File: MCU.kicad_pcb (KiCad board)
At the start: 4 copper layers, 110.3 x 131.5 mm, 135 parts, among them J1 HSEC8-150-01-X-RA-X, J10 Conn_02x10_Odd_Even, J11 Conn_01x10, J12 Conn_01x10, J13 Conn_01x10, J14 Conn_01x10, J15 Conn_01x02, J16 Conn_02x10_Odd_Even, J17 Conn_02x30_Counter_Clockwise, J18 Conn_01x10, J19 Conn_01x10, J2 Barrel_Jack_MountingPin, J20 Conn_01x02, J21 Conn_02x10_Odd_Even, J22 Conn_01x02, J32 Conn_01x02, J4 Conn_02x30_Counter_Clockwise, J5 Conn_02x10_Odd_Even, J6 Conn_01x02, J7 Conn_01x10, J8 Conn_01x10, J9 Conn_01x02, U1 TPS76333, U10 TXB0104RUT, U11 TPS76333, U12 TXB0104RUT, U13 TXB0104RUT, U14 TPS76333, U2 TXB0104RUT, U3 LMR36510ADDA, U5 TXB0104RUT, U6 TXB0104RUT, U7 TXB0104RUT, U8 TPS76333, U9 TXB0104RUT

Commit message: Ready for review
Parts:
- removed R13, R14, R15, R16, R17, R18, R19, R20, R21, R22, R23, R24, R25, R26, R27, R28, R44, R47, R50, R52, R53, R54, R55, R56, R69, R70, R71, R72, R73, R74, R75, R76: 0R, Resistor_SMD:R_0201_0603Metric
- added H6: MountingHole_Pad, MountingHole:MountingHole_2.2mm_M2_DIN965_Pad, F.Cu at (184.5, 149.0)
- added J23: Conn_01x02, Connector_PinHeader_2.54mm:PinHeader_1x02_P2.54mm_Vertical, F.Cu at (156.3, 136.3)
- moved H1 63.8 mm to (94.5, 147.5)
- moved H4 2.55 mm to (157.0, 146.5)
- moved H5 2.50 mm to (84.5, 147.5)
- moved J2 1.00 mm to (137.5, 140.5)
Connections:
- J1 pad 16: unconnected-(J1-Pad16) -> A0V
- J1 pad 20: BTN_TRIP_TEST -> unconnected-(J1-Pad20)
- J1 pad 28: unconnected-(J1-Pad28) -> A0V
- J1 pad 29: unconnected-(J1-Pad29) -> A0V
- J1 pad 35: unconnected-(J1-Pad35) -> A0V
- J1 pad 59: unconnected-(J1-Pad59) -> A0V
- J1 pad 62: unconnected-(J1-Pad62) -> A0V
- J1 pad 68: unconnected-(J1-Pad68) -> A0V
- J1 pad 74: unconnected-(J1-Pad74) -> A0V
- J1 pad 78: unconnected-(J1-Pad78) -> A0V
- J1 pad 88: unconnected-(J1-Pad88) -> A0V
- J1 pad 91: unconnected-(J1-Pad91) -> A0V
- J1 pad 94: unconnected-(J1-Pad94) -> A0V
- J17 pad 26: /GP_SUB3/TP7_Pin11 -> /GP_SUB3/P11
- J17 pad 27: /GP_SUB3/TP15_Pin12 -> /GP_SUB3/P12
- J17 pad 28: /GP_SUB3/TP8_Pin13 -> /GP_SUB3/P13
- J17 pad 5: /GP_SUB2/TP7_Pin11 -> /GP_SUB2/P11
- J17 pad 6: /GP_SUB2/TP15_Pin12 -> /GP_SUB2/P12
- J17 pad 7: /GP_SUB2/TP8_Pin13 -> /GP_SUB2/P13
- J4 pad 38: BTN_TRIP_TEST -> unconnected-(J4-Pin_38-Pad38)
- J4 pad 5: /GP_SUB/TP7_Pin11 -> /GP_SUB/P11
- J4 pad 54: /GP_SUB1/TP8_Pin13 -> /GP_SUB1/P13
- J4 pad 55: /GP_SUB1/TP15_Pin12 -> /GP_SUB1/P12
- J4 pad 56: /GP_SUB1/TP7_Pin11 -> /GP_SUB1/P11
- J4 pad 6: /GP_SUB/TP15_Pin12 -> /GP_SUB/P12
- J4 pad 7: /GP_SUB/TP8_Pin13 -> /GP_SUB/P13
- U10 pad 10: /GP_SUB2/TP7_Pin11 -> unconnected-(U10-B1-Pad10)
- U10 pad 2: Net-(U10-A1) -> unconnected-(U10-A1-Pad2)
- U10 pad 3: Net-(U10-A2) -> /GP_SUB2/P9
- U10 pad 4: Net-(U10-A3) -> unconnected-(U10-A3-Pad4)
- U10 pad 5: Net-(U10-A4) -> /GP_SUB2/P8
- U10 pad 8: /GP_SUB2/TP8_Pin13 -> unconnected-(U10-B3-Pad8)
- U12 pad 2: Net-(U12-A1) -> /GP_SUB3/P14
- U12 pad 3: Net-(U12-A2) -> /GP_SUB3/P16
- U12 pad 4: Net-(U12-A3) -> unconnected-(U12-A3-Pad4)
- U12 pad 5: Net-(U12-A4) -> /GP_SUB3/P7
- U12 pad 8: /GP_SUB3/TP15_Pin12 -> unconnected-(U12-B3-Pad8)
- U13 pad 10: /GP_SUB3/TP7_Pin11 -> unconnected-(U13-B1-Pad10)
- U13 pad 2: Net-(U13-A1) -> unconnected-(U13-A1-Pad2)
- U13 pad 3: Net-(U13-A2) -> /GP_SUB3/P9
- U13 pad 4: Net-(U13-A3) -> unconnected-(U13-A3-Pad4)
- U13 pad 5: Net-(U13-A4) -> /GP_SUB3/P8
- U13 pad 8: /GP_SUB3/TP8_Pin13 -> unconnected-(U13-B3-Pad8)
- U2 pad 2: Net-(U2-A1) -> /GP_SUB/P14
- U2 pad 3: Net-(U2-A2) -> /GP_SUB/P16
- U2 pad 4: Net-(U2-A3) -> unconnected-(U2-A3-Pad4)
- U2 pad 5: Net-(U2-A4) -> /GP_SUB/P7
- U2 pad 8: /GP_SUB/TP15_Pin12 -> unconnected-(U2-B3-Pad8)
- U5 pad 10: /GP_SUB/TP7_Pin11 -> unconnected-(U5-B1-Pad10)
- U5 pad 2: Net-(U5-A1) -> unconnected-(U5-A1-Pad2)
- U5 pad 3: Net-(U5-A2) -> /GP_SUB/P9
- U5 pad 4: Net-(U5-A3) -> unconnected-(U5-A3-Pad4)
- U5 pad 5: Net-(U5-A4) -> /GP_SUB/P8
- U5 pad 8: /GP_SUB/TP8_Pin13 -> unconnected-(U5-B3-Pad8)
- U6 pad 2: Net-(U6-A1) -> /GP_SUB1/P14
- U6 pad 3: Net-(U6-A2) -> /GP_SUB1/P16
- U6 pad 4: Net-(U6-A3) -> unconnected-(U6-A3-Pad4)
- U6 pad 5: Net-(U6-A4) -> /GP_SUB1/P7
- U6 pad 8: /GP_SUB1/TP15_Pin12 -> unconnected-(U6-B3-Pad8)
- U7 pad 10: /GP_SUB1/TP7_Pin11 -> unconnected-(U7-B1-Pad10)
- U7 pad 2: Net-(U7-A1) -> unconnected-(U7-A1-Pad2)
- U7 pad 3: Net-(U7-A2) -> /GP_SUB1/P9
- U7 pad 4: Net-(U7-A3) -> unconnected-(U7-A3-Pad4)
- U7 pad 5: Net-(U7-A4) -> /GP_SUB1/P8
- U7 pad 8: /GP_SUB1/TP8_Pin13 -> unconnected-(U7-B3-Pad8)
- U9 pad 2: Net-(U9-A1) -> /GP_SUB2/P14
- U9 pad 3: Net-(U9-A2) -> /GP_SUB2/P16
- U9 pad 4: Net-(U9-A3) -> unconnected-(U9-A3-Pad4)
- U9 pad 5: Net-(U9-A4) -> /GP_SUB2/P7
- U9 pad 8: /GP_SUB2/TP15_Pin12 -> unconnected-(U9-B3-Pad8)
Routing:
- net BTN_TRIP_TEST: track 187.6 -> 0.00 mm, vias 3 -> 0
- net PADLOCK_OF: track 183.3 -> 237.6 mm, vias 1 -> 2
- net /GP_SUB/P13: track 29.4 -> 67.4 mm, vias 0 -> 1
- net /GP_SUB1/TP15_Pin12: track 36.5 -> 0.00 mm
- net /GP_SUB/P12: track 22.1 -> 53.6 mm, vias 0 -> 2
- net /GP_SUB1/P13: track 33.3 -> 64.6 mm, vias 0 -> 1
- net /GP_SUB/TP8_Pin13: track 31.0 -> 0.00 mm, vias 1 -> 0
- net /GP_SUB/P11: track 25.1 -> 56.0 mm, vias 0 -> 2
- net /GP_SUB3/P11: track 37.3 -> 66.8 mm, vias 0 -> 1
- net /GP_SUB1/TP8_Pin13: track 29.2 -> 0.00 mm, vias 1 -> 0
- net /GP_SUB/TP7_Pin11: track 29.2 -> 0.00 mm, vias 1 -> 0
- net /GP_SUB3/P12: track 57.1 -> 85.8 mm, vias 0 -> 2
- net /GP_SUB1/P11: track 28.9 -> 57.2 mm, vias 0 -> 1
- net /GP_SUB/TP15_Pin12: track 28.0 -> 0.00 mm, vias 1 -> 0
- net /GP_SUB3/TP7_Pin11: track 23.8 -> 0.00 mm, vias 1 -> 0
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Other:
- board size 110.3 x 131.5 mm -> 110.3 x 131 mm
- board text added: "P24V"
- board text added: "PADL"
- board text added: "SHLD GND"
- board text removed: "VBUS"

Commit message: For review
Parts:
- added TP1: TestPoint, TestPoint:TestPoint_Pad_1.5x1.5mm, F.Cu at (133.2, 133.9)
- R68, R8, R88, R92: value 1k -> 4k7
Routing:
- net Net-(U3-PG): track 3.57 -> 12.7 mm
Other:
- board text added: "5VPG"
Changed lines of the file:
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@@
 			)
 		)
-		(property "Value" "1k"
+		(property "Value" "4k7"
 			(at 0 1.43 90)
 			(layer "F.Fab")
@@
 		(tags "capacitor")
 		(property "Reference" "C35"
-			(at 4 0 180)
+			(at 4 -1 180)
 			(layer "F.SilkS")
 			(effects
@@
 			)
 		)
-		(property "Value" "1k"
+		(property "Value" "4k7"
 			(at 0 1.43 90)
 			(layer "F.Fab")
@@
 			)
 		)
-		(property "Value" "1k"
+		(property "Value" "4k7"
 			(at 0 1.43 90)
 			(layer "F.Fab")
@@
 		)
 	)
+	(footprint "TestPoint:TestPoint_Pad_1.5x1.5mm"
+		(layer "F.Cu")
+		(at 133.225 133.925)
+		(descr "SMD rectangular pad as test Point, square 1.5mm side length")
+		(tags "test point SMD pad rectangle square")
+		(property "Reference" "TP1"
+			(at 0 -1.648 0)
+			(layer "F.SilkS")
+			(effects
+				(font
+					(size 1 1)
+					(thickness 0.15)
+				)
+			)
+		)
+		(property "Value" "TestPoint"
+			(at 0 1.75 0)
+			(layer "F.Fab")
+			(effects
+				(font
+					(size 1 1)
+					(thickness 0.15)
+				)
+			)
+		)
+		(property "Datasheet" ""
+			(at 0 0 0)
+			(unlocked yes)
+			(layer "F.Fab")
+			(hide yes)
+			(effects
+				(font
+					(size 1.27 1.27)
+					(thickness 0.15)
+				)
+			)
+		)
+		(property "Description" "test point"
+			(at 0 0 0)
+			(unlocked yes)
+			(layer "F.Fab")
+			(hide yes)
+			(effects
+				(font
+					(size 1.27 1.27)
+					(thickness 0.15)
+				)
+			)
+		)
+		(property ki_fp_filters "Pin* Test*")
+		(sheetname "/")
+		(sheetfile "MCU.kicad_sch")
+		(units
+			(unit
+				(name "A")
+				(pins "1")
+			)
+		)
+		(duplicate_pad_numbers_are_jumpers no)
+		(fp_line
+			(start -0.95 -0.95)
+			(end 0.95 -0.95)
+			(stroke
+				(width 0.12)
+				(type solid)
+			)
+			(layer "F.SilkS")
+		)
+		(fp_line
+			(start -0.95 0.95)
+			(end -0.95 -0.95)
+			(stroke
+				(width 0.12)
+				(type solid)
+			)
+			(layer "F.SilkS")
+		)
+		(fp_line
+			(start 0.95 -0.95)
+			(end 0.95 0.95)
+			(stroke
+				(width 0.12)
+				(type solid)
+			)
+			(layer "F.SilkS")
+		)
+		(fp_line
+			(start 0.95 0.95)
+			(end -0.95 0.95)
+			(stroke
+				(width 0.12)
+				(type solid)
+			)
+			(layer "F.SilkS")
+		)
+		(fp_line
+			(start -1.25 -1.25)
+			(end -1.25 1.25)
+			(stroke
+				(width 0.05)
+				(type solid)
+			)
+			(layer "F.CrtYd")
+		)
+		(fp_line
+			(start -1.25 -1.25)
+			(end 1.25 -1.25)
+			(stroke
+				(width 0.05)
+				(type solid)
+			)
+			(layer "F.CrtYd")
+		)
+		(fp_line
+			(start 1.25 1.25)
+			(end -1.25 1.25)
+			(stroke
+				(width 0.05)
+				(type solid)
+			)
+			(layer "F.CrtYd")
+		)
+		(fp_line
+			(start 1.25 1.25)
+			(end 1.25 -1.25)
+			(stroke
+				(width 0.05)
+				(type solid)
+			)
+			(layer "F.CrtYd")
+		)
+		(fp_text user "${REFERENCE}"
+			(at 0 -1.65 0)
+			(layer "F.Fab")
+			(effects
+				(font
+					(size 1 1)
+					(thickness 0.15)
+				)
+			)
+		)
+		(pad "1" smd rect
+			(at 0 0)
+			(size 1.5 1.5)
+			(layers "F.Cu" "F.Mask")
+			(net "Net-(U3-PG)")
+			(pinfunction "1_1")
+			(pintype "passive")
+		)
+		(embedded_fonts no)
+	)
 	(footprint "Resistor_SMD:R_0603_1608Metric"
 		(layer "F.Cu")
@@
 		(tags "resistor")
 		(property "Reference" "R98"
-			(at -2.5 1.5 180)
+			(at -3.5 2 270)
 			(layer "F.SilkS")
 			(effects
@@
 			)
 		)
-		(property "Value" "1k"
+		(property "Value" "4k7"
 			(at 0 1.43 0)
 			(layer "F.Fab")
@@
 		)
 	)
+	(gr_text "5VPG"
+		(at 134.5 135 0)
+		(layer "F.SilkS")
+		(effects
+			(font
+				(size 1.5 1.5)
+				(thickness 0.3)
+				(bold yes)
+			)
+			(justify left bottom)
+		)
+	)
 	(gr_text "P24V"
 		(at 147.5 141 0)
@@
 	)
 	(segment
-		(start 127 137)
-		(end 127.5 136.5)
-		(width 0.5)
-		(layer "F.Cu")
-		(net "A0V")
-	)
-	(segment
 		(start 109.6 84.2)
 		(end 109.6 84.9375)
@@
 	)
 	(segment
-		(start 127 137.52)
-		(end 127 137)
-		(width 0.5)
-		(layer "F.Cu")
-		(net "A0V")
-	)
-	(segment
 		(start 98.5 36.2)
 		(end 98.5 35.640488)
@@
 	)
 	(segment
+		(start 127.5 136.5)
+		(end 127 137)
+		(width 0.5)
+		(layer "F.Cu")
+		(net "A0V")
+	)
+	(segment
 		(start 93.769 87.558476)
 		(end 94.431524 88.221)
@@
 	)
 	(segment
-		(start 125.5 135.675)
-		(end 126.675 135.675)
-		(width 0.5)
-		(layer "F.Cu")
-		(net "A0V")
-	)
-	(segment
 		(start 156.7105 81.2205)
 		(end 157.099 81.609)
@@
 	)
 	(segment
-		(start 126.675 135.675)
-		(end 127 136)
-		(width 0.5)
-		(layer "F.Cu")
-		(net "A0V")
-	)
-	(segment
 		(start 156.08326 113.912314)
 		(end 156.894074 113.1015)
@@
 	)
 	(segment
+		(start 127 135.35)
+		(end 126.675 135.675)
+		(width 0.5)
+		(layer "F.Cu")
+		(net "A0V")
+	)
+	(segment
 		(start 161.27676 103.689)
 		(end 161.27676 103.224)
@@
 	)
 	(segment
+		(start 126.675 135.675)
+		(end 125.5 135.675)
+		(width 0.5)
+		(layer "F.Cu")
+		(net "A0V")
+	)
+	(segment
 		(start 109.64 118.81)
 		(end 109.64 119.275)
@@
 	)
 	(segment
+		(start 127 135.08)
+		(end 127 135.35)
+		(width 0.5)
+		(layer "F.Cu")
+		(net "A0V")
+	)
+	(segment
 		(start 161.4625 83.2559)
 		(end 161.4625 84.3955)
@@
 	)
 	(segment
+		(start 127 137)
+		(end 127 137.52)
+		(width 0.5)
+		(layer "F.Cu")
+		(net "A0V")
+	)
+	(segment
 		(start 160.15 75.5)
 		(end 160.075 75.575)
@@
 	)
 	(via
-		(at 127 136)
+		(at 127 135.08)
 		(size 0.6)
 		(drill 0.3)
@@
 	)
 	(segment
+		(start 129.174533 133.925)
+		(end 125.774533 137.325)
+		(width 0.2)
+		(layer "F.Cu")
+		(net "Net-(U3-PG)")
+	)
+	(segment
 		(start 124.175 137.325)
 		(end 124 137.15)
@@
 		(layer "F.Cu")
 		(net "Net-(U3-PG)")
+	)
+	(segment
+		(start 133.225 133.925)
+		(end 129.174533 133.925)
+		(width 0.2)
+		(layer "F.Cu")
+		(net "Net-(U3-PG)")
+	)
+	(segment
+		(start 125.774533 137.325)
+		(end 125.5 137.325)
+		(width 0.2)
+		(layer "F.Cu")
+		(net "Net-(U3-PG)")

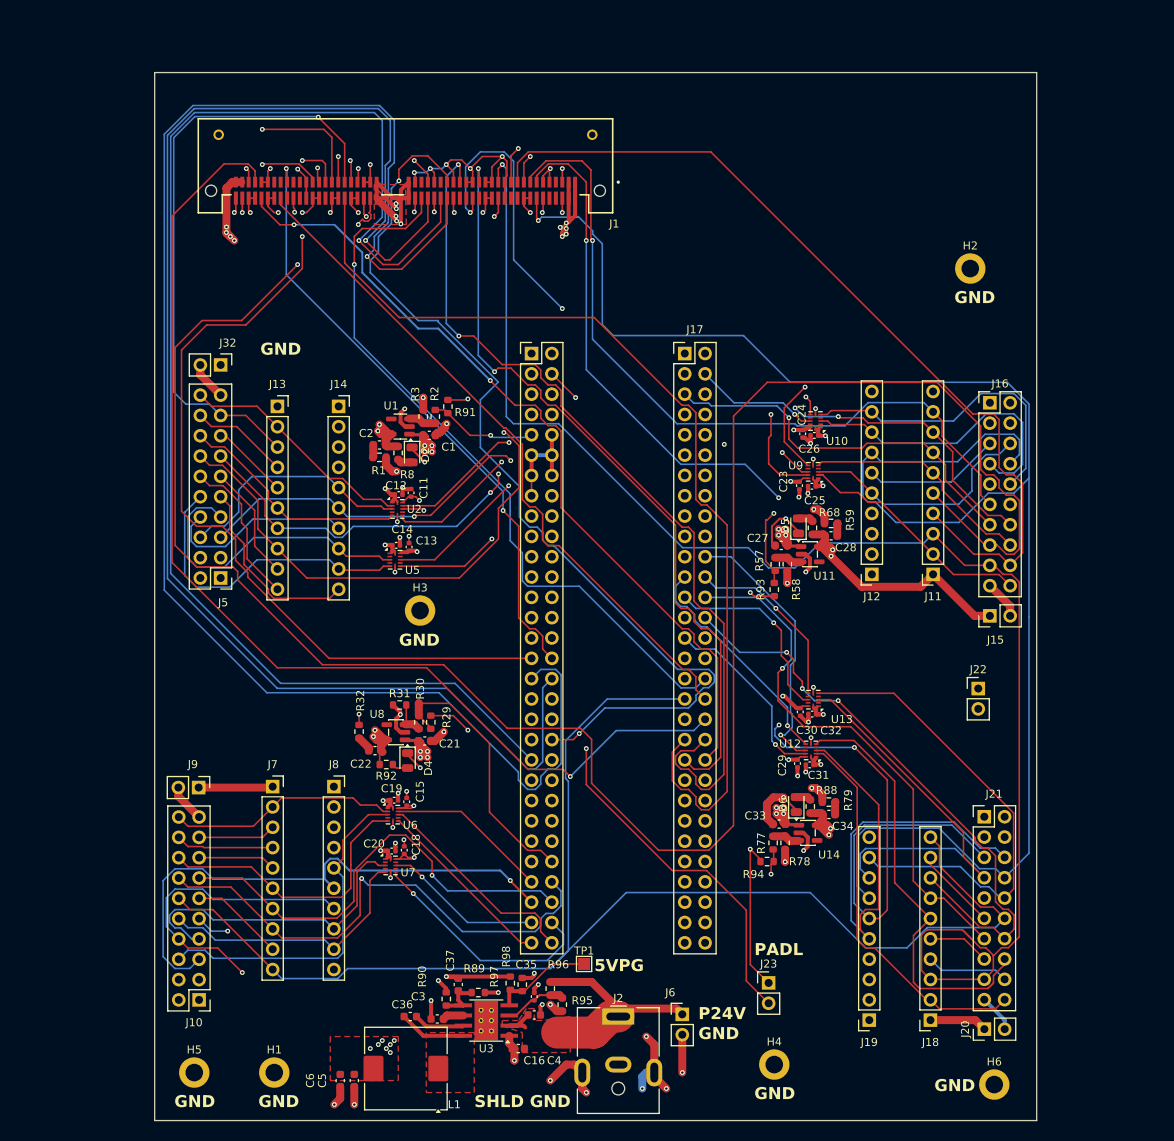
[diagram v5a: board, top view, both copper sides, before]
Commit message: Refactor GreenPak Pinout
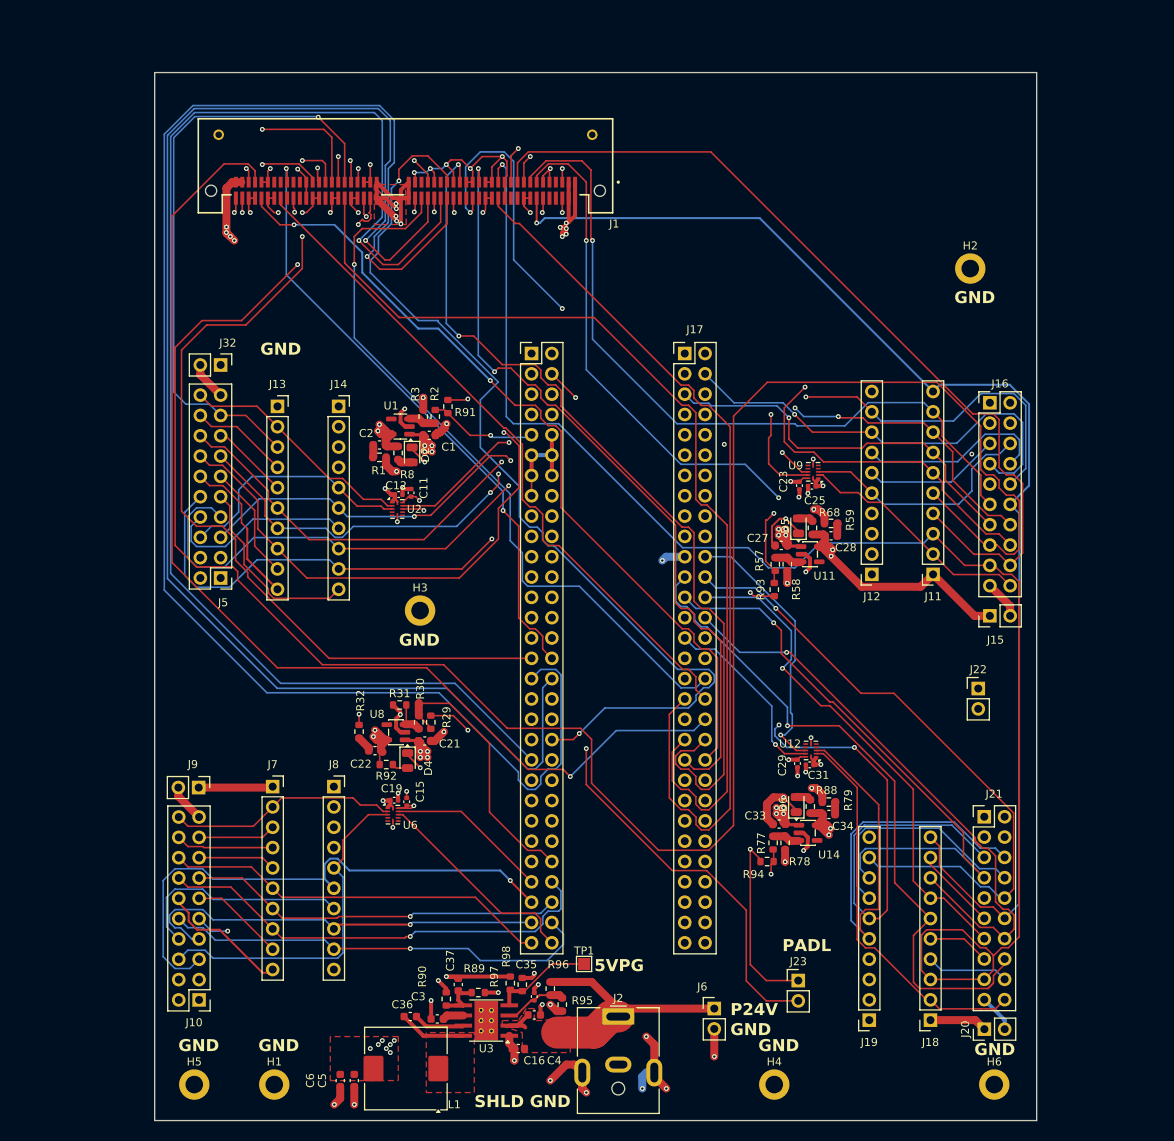
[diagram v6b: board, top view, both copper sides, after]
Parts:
- removed C13, C14, C18, C20, C24, C26, C30, C32: 100nF, Capacitor_SMD:C_0402_1005Metric
- removed U10, U13, U5, U7: TXB0104RUT, Package_DFN_QFN:Texas_R-PUQFN-N12
- moved J6 4.07 mm to (149.5, 139.5)
- moved J23 3.72 mm to (160.0, 136.0)
- moved H4 2.50 mm to (157.0, 149.0)
- moved H1 1.50 mm to (94.5, 149.0)
- moved H5 1.50 mm to (84.5, 149.0)
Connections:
- net /GP_SUB/P11 renamed /GP_SUB/P11_EN_PSD
- net /GP_SUB/P12 renamed /GP_SUB/P12_GP_OPCL_T2
- net /GP_SUB/P13 renamed /GP_SUB/P13_GP_OPCL_T1
- net /GP_SUB/P14 renamed /GP_SUB/P14_PG_PSD
- net /GP_SUB/P16 renamed /GP_SUB/P16_FET_OCF
- net /GP_SUB1/P11 renamed /GP_SUB1/P11_EN_PSD
- net /GP_SUB1/P12 renamed /GP_SUB1/P12_GP_OPCL_T2
- net /GP_SUB1/P13 renamed /GP_SUB1/P13_GP_OPCL_T1
- net /GP_SUB1/P14 renamed /GP_SUB1/P14_PG_PSD
- net /GP_SUB1/P16 renamed /GP_SUB1/P16_FET_OCF
- net /GP_SUB2/P11 renamed /GP_SUB2/P11_EN_PSD
- net /GP_SUB2/P12 renamed /GP_SUB2/P12_GP_OPCL_T2
- net /GP_SUB2/P13 renamed /GP_SUB2/P13_GP_OPCL_T1
- net /GP_SUB2/P14 renamed /GP_SUB2/P14_PG_PSD
- net /GP_SUB2/P16 renamed /GP_SUB2/P16_FET_OCF
- net /GP_SUB3/P11 renamed /GP_SUB3/P11_EN_PSD
- net /GP_SUB3/P12 renamed /GP_SUB3/P12_GP_OPCL_T2
- net /GP_SUB3/P13 renamed /GP_SUB3/P13_GP_OPCL_T1
- net /GP_SUB3/P14 renamed /GP_SUB3/P14_PG_PSD
- net /GP_SUB3/P16 renamed /GP_SUB3/P16_FET_OCF
- J10 pad 10: /GP_SUB1/P8 -> /GP_SUB1/P8_VIMOSA2
- J10 pad 12: SDMOS -> OPCL_US
- J10 pad 16: /GP_SUB1/P7 -> /GP_SUB1/P7_VIMOSA1
- J10 pad 7: /GP_SUB1/P9 -> /GP_SUB1/P9_VTMP
- J10 pad 8: OPCL_US -> /GP_SUB1/P10_SPARE
- J11 pad 10: SDMOS -> OPCL_DS
- J11 pad 6: /GP_SUB2/P7 -> /GP_SUB2/P7_VIMOSA1
- J12 pad 7: OPCL_DS -> /GP_SUB2/P10_SPARE
- J12 pad 8: /GP_SUB2/P9 -> /GP_SUB2/P9_VTMP
- J12 pad 9: /GP_SUB2/P8 -> /GP_SUB2/P8_VIMOSA2
- J13 pad 10: SDMOS -> OPCL_US
- J13 pad 6: /GP_SUB/P7 -> /GP_SUB/P7_VIMOSA1
- J14 pad 7: OPCL_US -> /GP_SUB/P10_SPARE
- J14 pad 8: /GP_SUB/P9 -> /GP_SUB/P9_VTMP
- J14 pad 9: /GP_SUB/P8 -> /GP_SUB/P8_VIMOSA2
- J16 pad 10: /GP_SUB2/P8 -> /GP_SUB2/P8_VIMOSA2
- J16 pad 12: SDMOS -> OPCL_DS
- J16 pad 16: /GP_SUB2/P7 -> /GP_SUB2/P7_VIMOSA1
- J16 pad 7: /GP_SUB2/P9 -> /GP_SUB2/P9_VTMP
- J16 pad 8: OPCL_DS -> /GP_SUB2/P10_SPARE
- J17 pad 2: /GP_SUB2/TP6_Pin7 -> /GP_SUB2/P7_VIMOSA1
- J17 pad 23: /GP_SUB3/TP6_Pin7 -> /GP_SUB3/P7_VIMOSA1
- J17 pad 24: /GP_SUB3/TP12_Pin8 -> /GP_SUB3/P8_VIMOSA2
- J17 pad 25: /GP_SUB3/TP13_Pin9 -> /GP_SUB3/P9_VTMP
- J17 pad 3: /GP_SUB2/TP12_Pin8 -> /GP_SUB2/P8_VIMOSA2
- J17 pad 4: /GP_SUB2/TP13_Pin9 -> /GP_SUB2/P9_VTMP
- J18 pad 10: SDMOS -> OPCL_DS
- J18 pad 6: /GP_SUB3/P7 -> /GP_SUB3/P7_VIMOSA1
- J19 pad 7: OPCL_DS -> /GP_SUB3/P10_SPARE
- J19 pad 8: /GP_SUB3/P9 -> /GP_SUB3/P9_VTMP
- J19 pad 9: /GP_SUB3/P8 -> /GP_SUB3/P8_VIMOSA2
- J21 pad 10: /GP_SUB3/P8 -> /GP_SUB3/P8_VIMOSA2
- J21 pad 12: SDMOS -> OPCL_DS
- J21 pad 16: /GP_SUB3/P7 -> /GP_SUB3/P7_VIMOSA1
- J21 pad 7: /GP_SUB3/P9 -> /GP_SUB3/P9_VTMP
- J21 pad 8: OPCL_DS -> /GP_SUB3/P10_SPARE
- J4 pad 2: /GP_SUB/TP6_Pin7 -> /GP_SUB/P7_VIMOSA1
- J4 pad 3: /GP_SUB/TP12_Pin8 -> /GP_SUB/P8_VIMOSA2
- J4 pad 4: /GP_SUB/TP13_Pin9 -> /GP_SUB/P9_VTMP
- J4 pad 57: /GP_SUB1/TP13_Pin9 -> /GP_SUB1/P9_VTMP
- J4 pad 58: /GP_SUB1/TP12_Pin8 -> /GP_SUB1/P8_VIMOSA2
- J4 pad 59: /GP_SUB1/TP6_Pin7 -> /GP_SUB1/P7_VIMOSA1
- J5 pad 10: /GP_SUB/P8 -> /GP_SUB/P8_VIMOSA2
- J5 pad 12: SDMOS -> OPCL_US
- J5 pad 16: /GP_SUB/P7 -> /GP_SUB/P7_VIMOSA1
- J5 pad 7: /GP_SUB/P9 -> /GP_SUB/P9_VTMP
- J5 pad 8: OPCL_US -> /GP_SUB/P10_SPARE
- J7 pad 10: SDMOS -> OPCL_US
- J7 pad 6: /GP_SUB1/P7 -> /GP_SUB1/P7_VIMOSA1
- J8 pad 7: OPCL_US -> /GP_SUB1/P10_SPARE
- J8 pad 8: /GP_SUB1/P9 -> /GP_SUB1/P9_VTMP
- J8 pad 9: /GP_SUB1/P8 -> /GP_SUB1/P8_VIMOSA2
- U12 pad 5: /GP_SUB3/P7 -> unconnected-(U12-A4-Pad5)
- U12 pad 7: /GP_SUB3/TP6_Pin7 -> unconnected-(U12-B4-Pad7)
- U2 pad 5: /GP_SUB/P7 -> unconnected-(U2-A4-Pad5)
- U2 pad 7: /GP_SUB/TP6_Pin7 -> unconnected-(U2-B4-Pad7)
- U6 pad 5: /GP_SUB1/P7 -> unconnected-(U6-A4-Pad5)
- U6 pad 7: /GP_SUB1/TP6_Pin7 -> unconnected-(U6-B4-Pad7)
- U9 pad 5: /GP_SUB2/P7 -> unconnected-(U9-A4-Pad5)
- U9 pad 7: /GP_SUB2/TP6_Pin7 -> unconnected-(U9-B4-Pad7)
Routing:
- net SDMOS: track 485.4 -> 113.8 mm, vias 1 -> 0
- net /GP_SUB3/P7_VIMOSA1: track 0.00 -> 85.0 mm, vias 0 -> 1
- net /GP_SUB3/P8_VIMOSA2: track 0.00 -> 80.9 mm, vias 0 -> 1
- net /GP_SUB/P8_VIMOSA2: track 0.00 -> 76.4 mm, vias 0 -> 1
- net /GP_SUB3/P9_VTMP: track 0.00 -> 76.2 mm, vias 0 -> 1
- net /GP_SUB/P9_VTMP: track 0.00 -> 76.2 mm, vias 0 -> 2
- net OPCL_DS: track 225.1 -> 156.6 mm
- net /GP_SUB/P7_VIMOSA1: track 0.00 -> 66.4 mm, vias 0 -> 1
- net /GP_SUB3/P8: track 60.7 -> 0.00 mm
- net /GP_SUB2/P8_VIMOSA2: track 0.00 -> 57.8 mm, vias 0 -> 1
- net /GP_SUB2/P7_VIMOSA1: track 0.00 -> 56.3 mm, vias 0 -> 1
- net /GP_SUB2/P9_VTMP: track 0.00 -> 55.5 mm, vias 0 -> 1
- net /GP_SUB3/P7: track 55.1 -> 0.00 mm
- net /GP_SUB1/P8_VIMOSA2: track 0.00 -> 54.5 mm, vias 0 -> 1
- net /GP_SUB3/P9: track 52.5 -> 0.00 mm
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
